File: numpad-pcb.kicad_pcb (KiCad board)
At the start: 2 copper layers, 76.2 x 118.8 mm, 62 parts, among them J1 AVR-ISP-6, SW1 SW_Push, SW10 7/home, SW11 4/left, SW12 8/up, SW13 5, SW14 9/pgup, SW15 6/right, SW16 +, SW18 1/end, SW19 0/insert, SW2 ESC, SW20 2/down, SW22 3/pgdn, SW23 ./delete, SW24 ENTER, SW3 TAB, SW4 BACKSPACE, SW5 FN, SW6 NUM_LOCK, SW7 /, SW8 *, SW9 -, U1 ATmega32U4-A, Y1 Crystal_GND24_Small

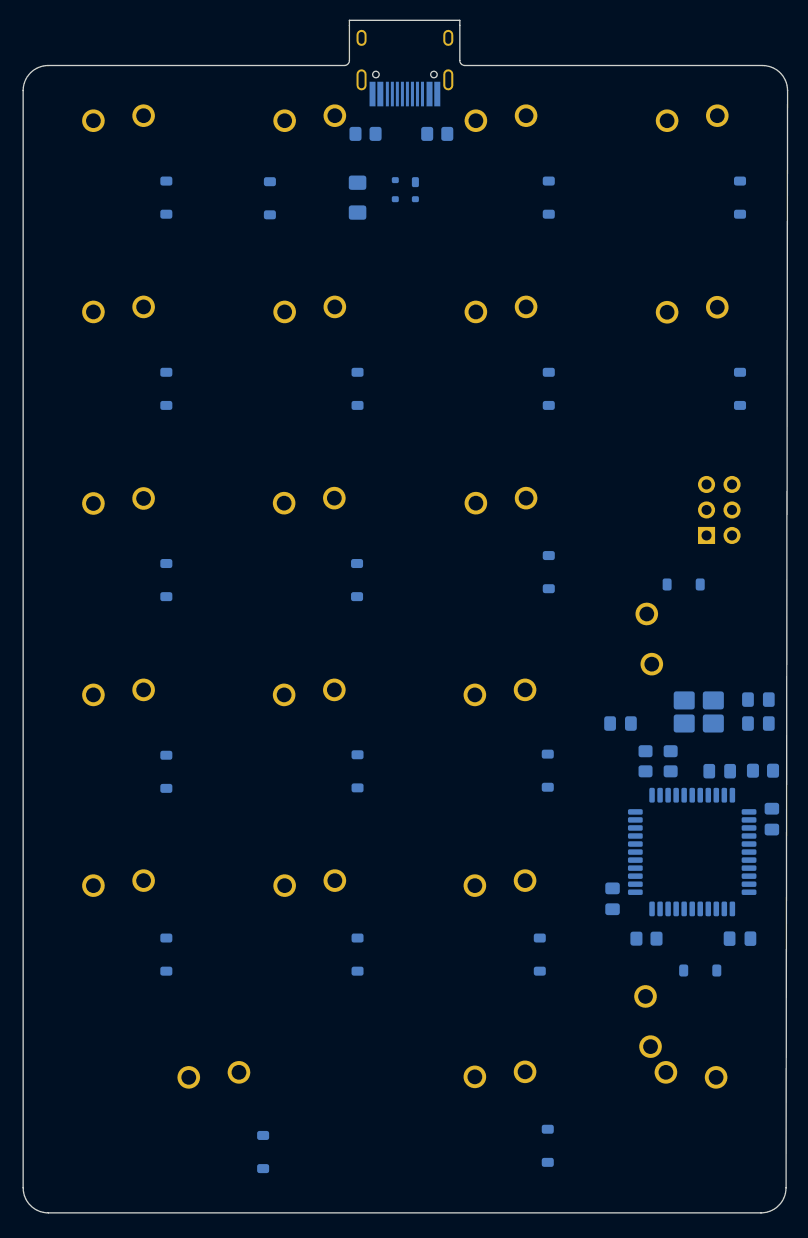
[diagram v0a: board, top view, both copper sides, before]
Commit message: Repair edge and bottom traces
Fixed the differential pair to have closer trace lengths (+/- 0.5 mm
reduced to 0.03 mm) for higher accuracy and error prevention. Also
created GND pour for crystal to reduce noise.
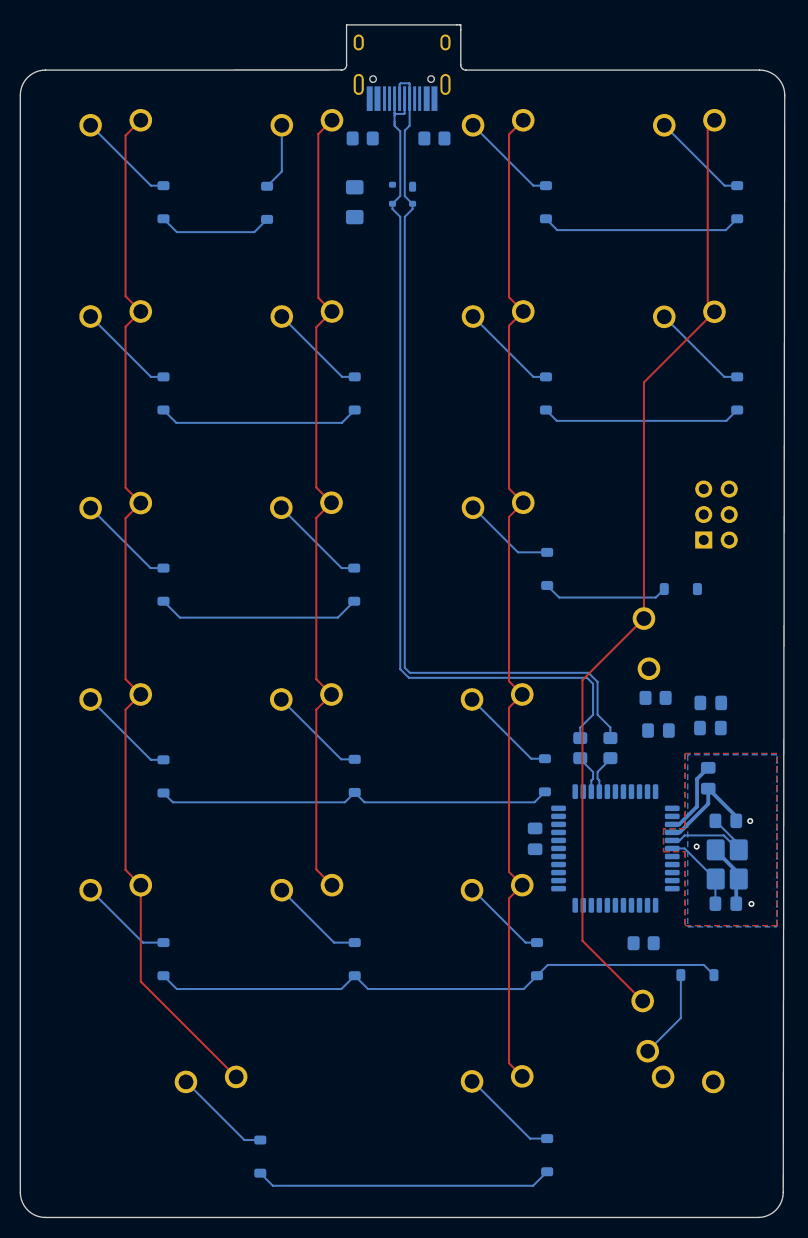
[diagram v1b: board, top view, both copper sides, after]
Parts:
- moved C1 22.3 mm to (113.3, 111.2)
- moved C6 20.6 mm to (120.0, 128.5)
- moved Y1 15.4 mm to (120.1, 124.6), turned to 90 degrees
- moved R4 12.9 mm to (113.0, 108.0)
- moved C7 10.2 mm to (120.0, 120.2)
- moved C3 9.76 mm to (101.0, 122.0)
- moved C4 8.97 mm to (118.5, 111.0)
- moved U1 7.66 mm to (109.0, 123.0)
- moved C2 7.53 mm to (118.2, 116.0)
- moved C5 6.86 mm to (118.5, 108.5)
- moved R3 6.63 mm to (105.5, 113.0)
- moved R2 6.14 mm to (108.5, 113.0), turned to 90 degrees
- moved D23 0.93 mm to (102.2, 153.6)
- moved D18 0.54 mm to (64.0, 134.0)
- moved D20 0.54 mm to (83.0, 134.0)
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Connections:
- R2 pad 1: Net-(U1-D+) -> D+
- R3 pad 2: Net-(U1-D-) -> D-
- U1 pad 3: Net-(U1-D-) -> D-
- U1 pad 4: Net-(U1-D+) -> D+
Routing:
- net COL0: track 0.00 -> 104.3 mm
- net COL2: track 0.00 -> 100.9 mm
- net COL3: track 0.00 -> 96.2 mm
- net D+: track 0.00 -> 91.4 mm
- net D-: track 0.00 -> 89.9 mm
- net COL1: track 0.00 -> 81.1 mm
- net ROW4: track 0.00 -> 57.9 mm
- net ROW1: track 0.00 -> 40.1 mm
- net ROW3: track 0.00 -> 39.6 mm
- net ROW2: track 0.00 -> 32.9 mm
- net ROW0: track 0.00 -> 31.4 mm
- net ROW5: track 0.00 -> 29.7 mm
- net GND: track 0.00 -> 17.2 mm, vias 0 -> 3
- net Net-(U1-XTAL2): track 0.00 -> 11.3 mm
- net Net-(D23-A): track 0.00 -> 9.84 mm
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- added copper zone on B.Cu, net GND
- added copper zone on F.Cu, net GND
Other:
- outline, holes or cut-outs redrawn

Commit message: Routed power
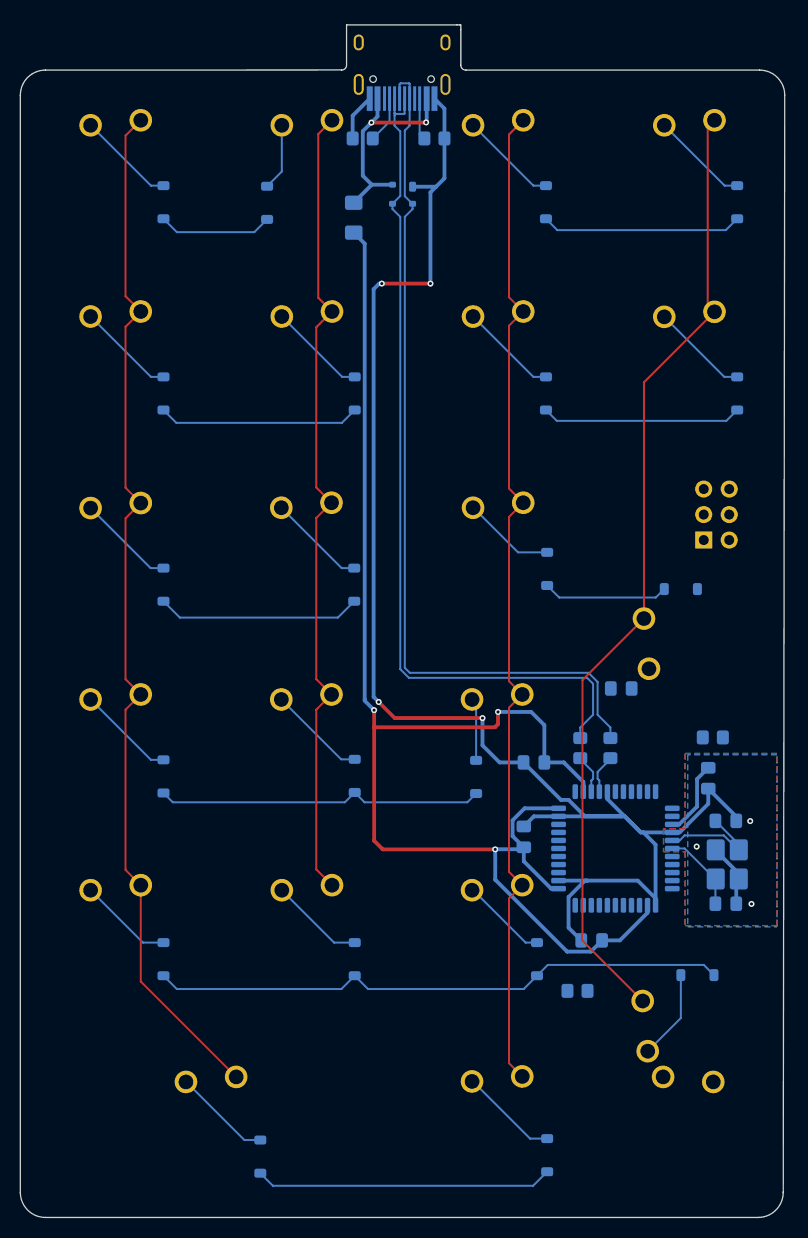
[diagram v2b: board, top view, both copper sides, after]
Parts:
- moved C4 24.2 mm to (106.6, 132.2)
- moved C5 18.6 mm to (100.9, 114.4)
- moved R1 8.12 mm to (105.2, 137.2)
- moved R4 6.93 mm to (118.7, 111.9)
- moved D15 6.86 mm to (95.1, 115.9)
- moved C1 5.59 mm to (109.6, 107.1)
- moved F1 1.55 mm to (82.9, 60.2)
- moved C3 1.14 mm to (99.9, 121.8)
- turned R5 to 0 degrees
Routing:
- net GND: track 17.2 -> 168.9 mm, vias 3 -> 7
- net +5V: track 7.53 -> 151.2 mm, vias 0 -> 3
- net VCC: track 0.00 -> 22.1 mm, vias 0 -> 2
- net ROW3: track 39.6 -> 32.7 mm
- net Net-(USB1-CC1): track 0.00 -> 4.66 mm
- net Net-(USB1-CC2): track 0.00 -> 4.16 mm
- net Net-(D15-A): track 9.71 -> 6.24 mm

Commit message: Finish traces and start silkscreen
Still need to modify traces to be more optimal and increase readibility.
Also updated silkscreen preferences locally to have the label of each
switch on both the front and back of the PCB. Need to make a note that
this change is local because of the submodule imported from the start.
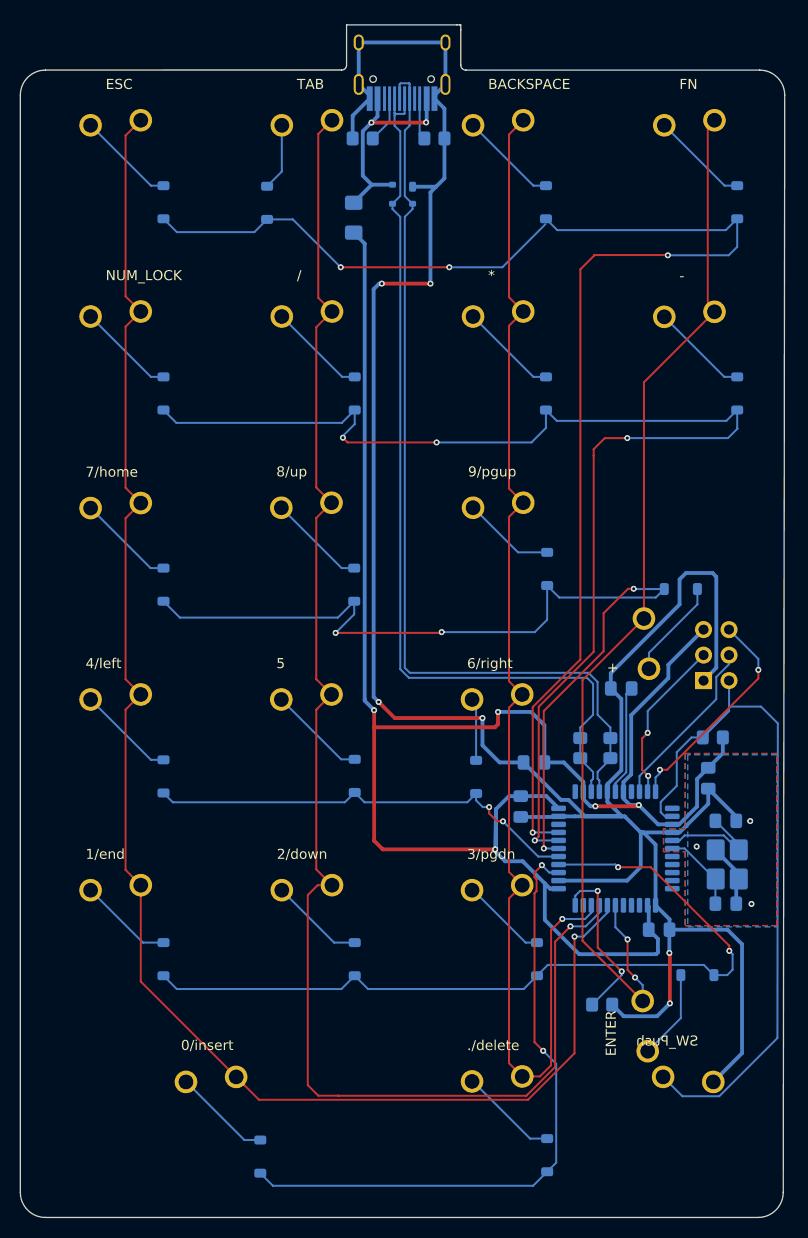
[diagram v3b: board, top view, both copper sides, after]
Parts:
- moved J1 14.0 mm to (119.0, 103.7)
- moved C4 6.81 mm to (113.4, 131.1), turned to 0 degrees
- moved C3 3.04 mm to (99.6, 118.8), turned to -90 degrees
- moved R1 2.81 mm to (107.7, 138.6), turned to 0 degrees
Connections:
- U1 pad 28: COL0 -> COL3
- U1 pad 29: COL1 -> COL0
- U1 pad 30: COL2 -> COL1
- U1 pad 31: COL3 -> COL2
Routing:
- net ROW0: track 31.4 -> 143.0 mm, vias 0 -> 4
- net GND: track 168.9 -> 260.7 mm, vias 7 -> 9
- net ROW1: track 40.1 -> 126.8 mm, vias 0 -> 4
- net RESET: track 0.00 -> 73.4 mm
- net COL1: track 81.1 -> 148.0 mm, vias 0 -> 1
- net ROW2: track 32.9 -> 96.3 mm, vias 0 -> 4
- net COL0: track 104.3 -> 157.5 mm, vias 0 -> 1
- net +5V: track 151.2 -> 191.7 mm, vias 3 -> 5
- net ROW5: track 29.7 -> 63.9 mm, vias 0 -> 2
- net ROW4: track 57.9 -> 82.9 mm, vias 0 -> 2
- net COL2: track 100.9 -> 123.2 mm, vias 0 -> 1
- net MISO: track 0.00 -> 22.0 mm, vias 0 -> 2
- net SCK: track 0.00 -> 17.3 mm
- net Net-(U1-~{HWB}/PE2): track 0.00 -> 16.9 mm, vias 0 -> 2
- net MOSI: track 0.00 -> 16.4 mm, vias 0 -> 2
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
